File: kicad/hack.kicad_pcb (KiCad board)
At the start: 2 copper layers, 27 parts, among them P1 USB_micro, P2 CONN_01X13, P3 CONN_01X13, U1 NCP1117, U2 STF202, U3 ATSAMD21E, U4 MRF24J40MA, X1 MC-306

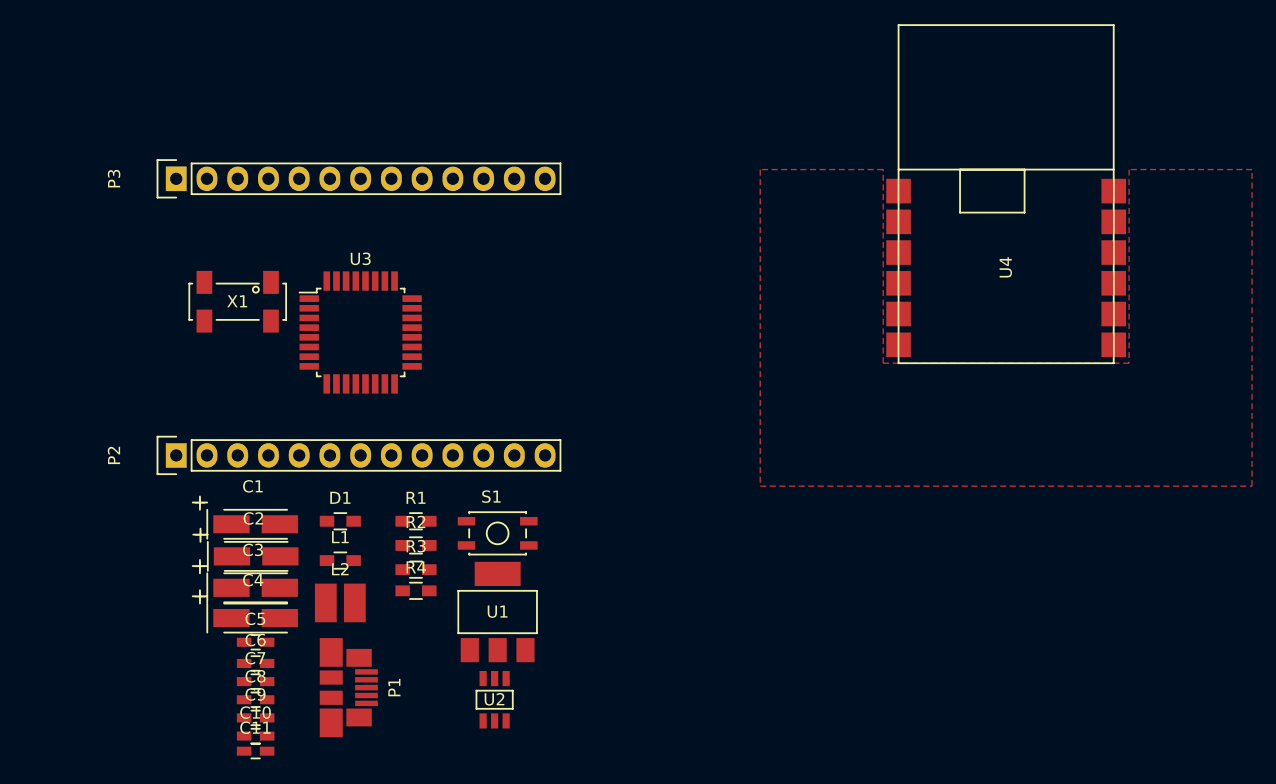
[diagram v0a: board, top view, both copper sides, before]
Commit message: Final components placement almost done
During this phase I checked if everything could fit in the board. It
didn't, so I found a replacement LDO (in a small 1.2x1.2mm DFN package)
that needs 2x0603 ceramic caps rather than two clunky electros (more
free space then) and I finally changed the D21E package to QFN as well,
now everything seems to fit quite well.
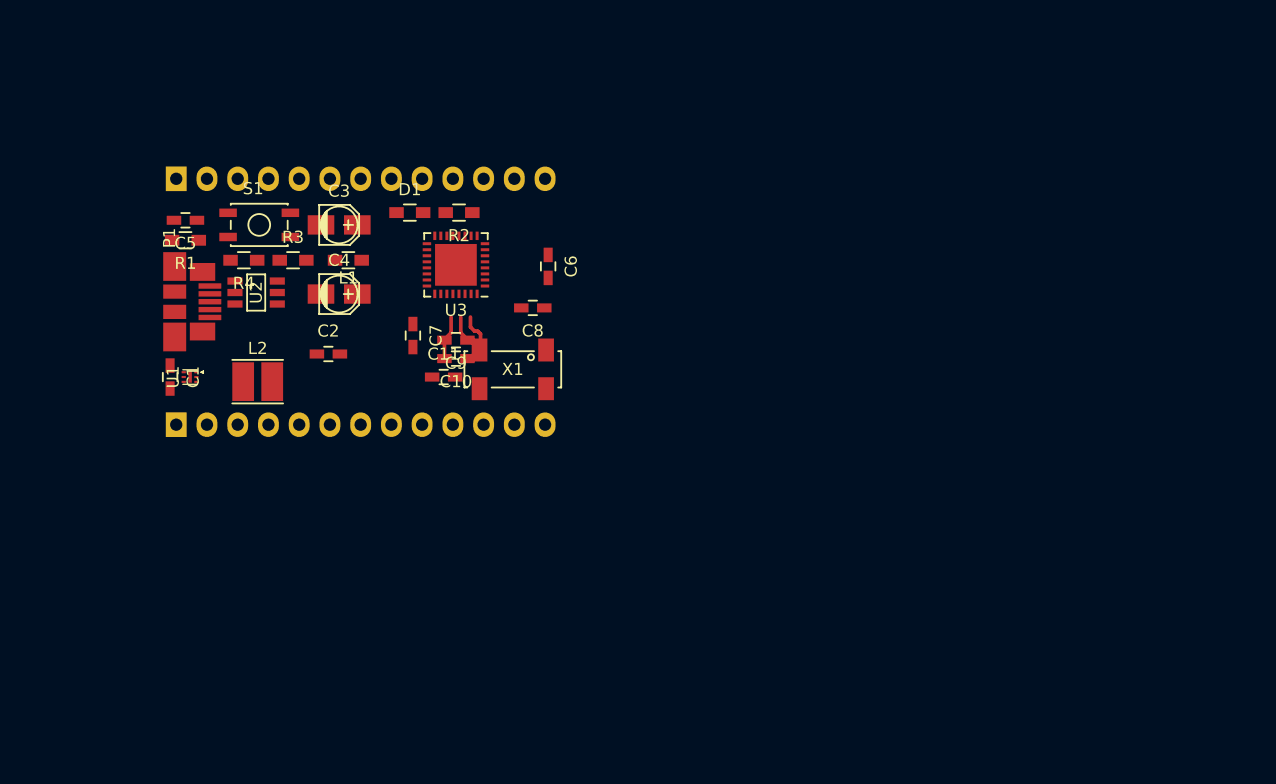
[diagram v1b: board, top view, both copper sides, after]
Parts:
- removed U4: MRF24J40MA, hack-footprints:MRF24J40MA
- C1, C2: value 10u -> 2.2u; footprint Capacitors_Tantalum_SMD:TantalC_SizeA_EIA-3216_HandSoldering -> Capacitors_SMD:C_0603_HandSoldering
- C3, C4: footprint Capacitors_Tantalum_SMD:TantalC_SizeA_EIA-3216_HandSoldering -> Capacitors_SMD:c_elec_3x5.3
- L2: footprint hack-footprints:ELLVFG -> ELLVFG
- P1: footprint hack-footprints:47346-0001 -> 47346-0001
- P2, P3: moved to B.Cu
- U1: value NCP1117 -> MIC5528; footprint hack-footprints:SOT-223 -> Housings_DFN_QFN:DFN-6-1EP_1.2x1.2mm_Pitch0.4mm
- U3: footprint Housings_QFP:TQFP-32_7x7mm_Pitch0.8mm -> QFN-32-1EP_5x5mm_Pitch0.5mm
- moved C6 40.8 mm to (185.7, 83.4), turned to 270 degrees
- moved C8 39.7 mm to (184.4, 86.9), turned to 180 degrees
- moved U2 39.0 mm to (161.5, 85.6), turned to 270 degrees
- moved C5 35.3 mm to (155.7, 79.6), turned to 180 degrees
- moved C9 35.3 mm to (178.1, 89.5), turned to 180 degrees
- moved C10 35.3 mm to (178.1, 91.1), turned to 180 degrees
- moved C11 34.6 mm to (177.0, 92.6)
- moved P1 34.4 mm to (154.8, 86.4)
- moved S1 32.2 mm to (161.8, 80.0)
- moved U1 32.0 mm to (156.1, 92.6), turned to 90 degrees
- moved C7 31.4 mm to (174.5, 89.2), turned to 270 degrees
- moved R4 30.8 mm to (160.5, 82.9), turned to 180 degrees
- moved C3 30.8 mm to (168.4, 80.0)
- moved R1 30.0 mm to (155.7, 81.3), turned to 180 degrees
- moved R2 27.7 mm to (178.3, 79.0), turned to 180 degrees
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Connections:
- net Net-(C3-Pad1) renamed VDDANA
- net Net-(C5-Pad2) renamed shield
- net Net-(C9-Pad1) renamed VDDCORE
- net USB-DM renamed USB-D-
- net USB-DP renamed USB-D+
- C1 pad 1: Net-(C1-Pad1) -> VBUS
- C2 pad 1: Net-(C2-Pad1) -> VDD
- L1 pad 1: Net-(L1-Pad1) -> VDD
- L2 pad 1: Net-(L2-Pad1) -> VDD
- P1 pad 1: Net-(P1-Pad1) -> VBUS
- R3 pad 2: Net-(R3-Pad2) -> VDDF
- U1 pad 1: GND -> VDD
- U1 pad 2: Net-(C2-Pad1) -> VDD
- U1 pad 3: Net-(C1-Pad1) -> GND
- U1 pad 4: Net-(C2-Pad1) -> Net-(U1-Pad4)
- U2 pad 1: Net-(P1-Pad1) -> VBUS
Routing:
- net GND: track 0.00 -> 6.60 mm
- net VDDCORE: track 0.00 -> 2.07 mm
- net VDDF: track 0.00 -> 1.44 mm
- removed copper zone on F.Cu, net GND
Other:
- net class Default: clearance 0.2 -> 0.1524; trace_width 0.25 -> 0.1524; via_dia 0.6 -> 0.508; via_drill 0.4 -> 0.3302
- net class Power added: clearance 0.1524, trace_width 0.3048, via_dia 0.5842, via_drill 0.3302
- rule trace_clearance: 0.2 -> 0.1524
- rule trace_min: 0.2 -> 0.1524
- rule via_min_drill: 0.3 -> 0.3302
- rule via_min_size: 0.4 -> 0.508

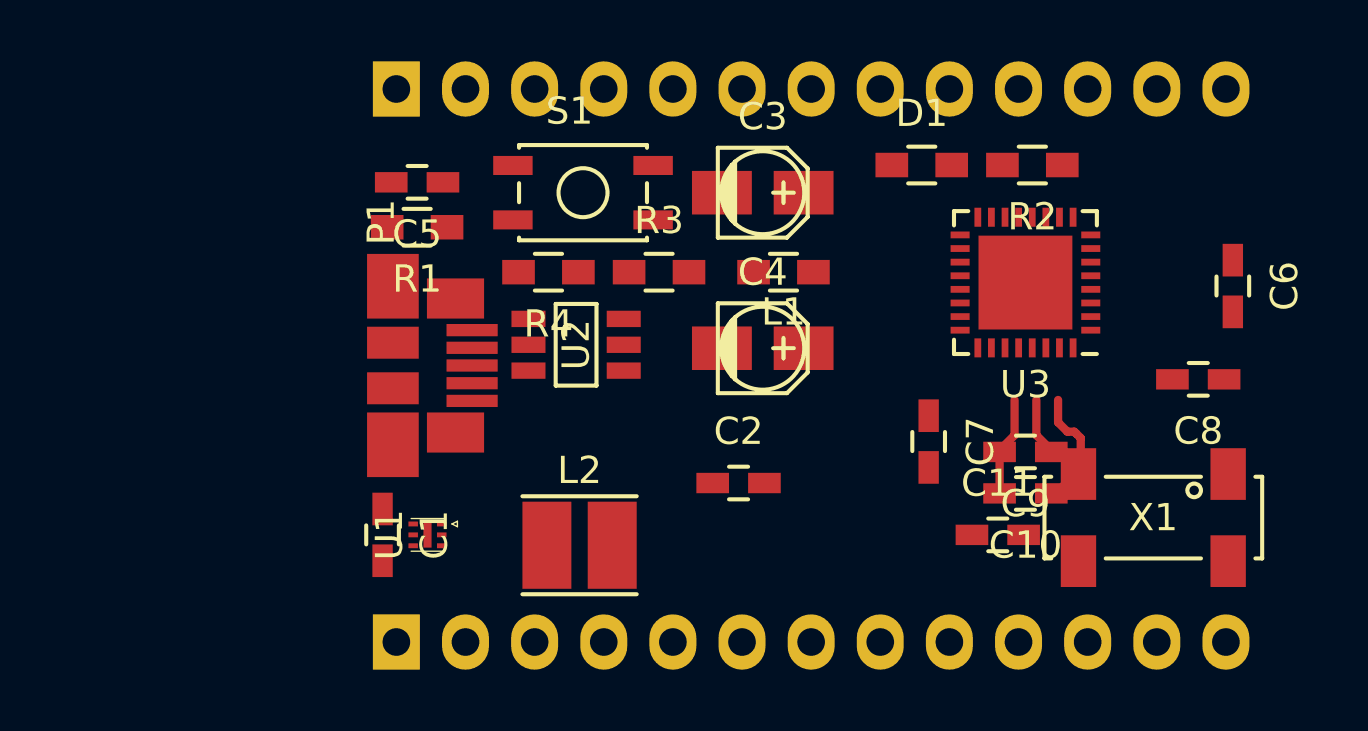
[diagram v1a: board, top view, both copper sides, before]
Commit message: Layout 99,9% finished
Nets 100% routed, need to double check if copper pours are all connected
to ground; added fiducials on board (for pick-n-place machines), I only
need to find a good spot for them
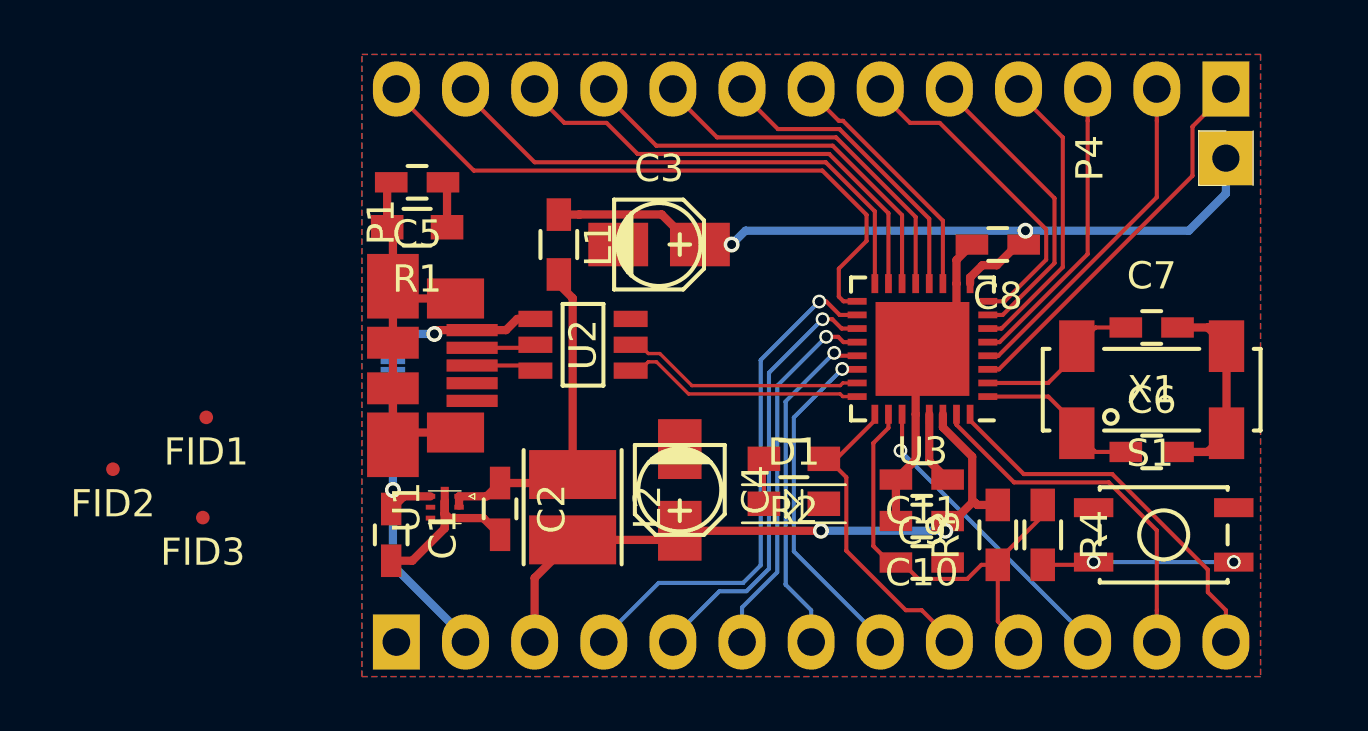
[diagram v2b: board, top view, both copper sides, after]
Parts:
- added FID1: FIDUCIAL, hack-footprints:FIDUCIAL, F.Cu at (148.0, 88.3)
- added FID2: FIDUCIAL, hack-footprints:FIDUCIAL, F.Cu at (144.5, 90.2)
- added FID3: FIDUCIAL, hack-footprints:FIDUCIAL, F.Cu at (147.8, 91.9)
- added JP1: Jumper_NO_Small, hack-footprints:SMD_Jumper, B.Cu at (154.8, 86.4)
- added P4: CONN_01X01, Pin_Headers:Pin_Header_Straight_1x01, F.Cu at (185.4, 78.7)
- D1: footprint Resistors_SMD:R_0603_HandSoldering -> hack-footprints:LED_0603_HandSoldering
- L1: footprint Resistors_SMD:R_0603_HandSoldering -> hack-footprints:L_0603_HandSoldering
- U1: footprint Housings_DFN_QFN:DFN-6-1EP_1.2x1.2mm_Pitch0.4mm -> hack-footprints:DFN-6-1EP_1.2x1.2mm_Pitch0.4mm
- moved P3 30.5 mm to (185.4, 76.2), turned to 90 degrees
- moved S1 24.8 mm to (183.1, 92.6)
- moved R4 20.6 mm to (178.7, 92.6), turned to 270 degrees
- moved R3 15.8 mm to (177.0, 92.6), turned to 90 degrees
- moved R2 13.9 mm to (169.5, 89.8)
- moved D1 13.3 mm to (169.5, 91.4)
- moved C7 9.20 mm to (182.7, 85.0), turned to 0 degrees
- moved C8 8.88 mm to (177.0, 81.9)
- moved C2 8.81 mm to (158.8, 91.6), turned to 270 degrees
- moved L1 8.32 mm to (160.9, 81.9), turned to 90 degrees
- moved C6 6.79 mm to (182.7, 89.5), turned to 0 degrees
- moved C4 6.03 mm to (165.4, 90.9), turned to 270 degrees
- moved X1 4.70 mm to (182.7, 87.2), turned to 0 degrees
- moved U3 4.50 mm to (174.3, 85.8)
- moved C3 4.26 mm to (164.6, 81.9)
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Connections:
- C1 pad 1: VBUS -> VLDO
- D1 pad 1: GND -> Net-(D1-Pad1)
- D1 pad 2: Net-(D1-Pad2) -> GND
- P2 pad 1: Net-(P2-Pad1) -> GND
- P2 pad 10: Net-(P2-Pad10) -> !RESET
- P2 pad 11: Net-(P2-Pad11) -> PA28
- P2 pad 12: Net-(P2-Pad12) -> PA30/SWCLK
- P2 pad 13: Net-(P2-Pad13) -> PA31/SWDIO
- P2 pad 2: Net-(P2-Pad2) -> VLDO
- P2 pad 3: Net-(P2-Pad3) -> VDDF
- P2 pad 4: Net-(P2-Pad4) -> PA17
- P2 pad 5: Net-(P2-Pad5) -> PA18
- P2 pad 6: Net-(P2-Pad6) -> PA19
- P2 pad 7: Net-(P2-Pad7) -> PA22
- P2 pad 8: Net-(P2-Pad8) -> PA23
- P2 pad 9: Net-(P2-Pad9) -> PA27
- P3 pad 1: Net-(P3-Pad1) -> PA02/A
- P3 pad 10: Net-(P3-Pad10) -> PA11
- P3 pad 11: Net-(P3-Pad11) -> PA14
- P3 pad 12: Net-(P3-Pad12) -> PA15
- P3 pad 13: Net-(P3-Pad13) -> PA16
- P3 pad 2: Net-(P3-Pad2) -> PA03/A
- P3 pad 3: Net-(P3-Pad3) -> PA04/A
- P3 pad 4: Net-(P3-Pad4) -> PA05/A
- P3 pad 5: Net-(P3-Pad5) -> PA06/A
- P3 pad 6: Net-(P3-Pad6) -> PA07/A
- P3 pad 7: Net-(P3-Pad7) -> PA08
- P3 pad 8: Net-(P3-Pad8) -> PA09
- P3 pad 9: Net-(P3-Pad9) -> PA10
- R2 pad 1: PA28 -> PA27
- R2 pad 2: Net-(D1-Pad2) -> Net-(D1-Pad1)
- U1 pad 6: VBUS -> VLDO
- U3 pad 33: (no net) -> GND
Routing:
- net VDDANA: track 0.00 -> 30.3 mm, vias 0 -> 2
- net PA16: track 0.00 -> 23.5 mm
- net VDDF: track 1.44 -> 24.4 mm, vias 0 -> 2
- net PA15: track 0.00 -> 19.6 mm
- net PA17: track 0.00 -> 19.2 mm, vias 0 -> 1
- net GND: track 6.60 -> 25.2 mm
- net PA14: track 0.00 -> 17.6 mm
- net !RESET: track 0.00 -> 16.4 mm
- net PA18: track 0.00 -> 16.1 mm, vias 0 -> 1
- net PA11: track 0.00 -> 15.5 mm
- net shield: track 0.00 -> 14.8 mm
- net PA31/SWDIO: track 0.00 -> 14.2 mm
- net PA02/A: track 0.00 -> 14.2 mm
- net PA19: track 0.00 -> 13.7 mm, vias 0 -> 1
- net PA30/SWCLK: track 0.00 -> 13.5 mm
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- added copper zone on B.Cu, net GND
- added copper zone on F.Cu, net GND

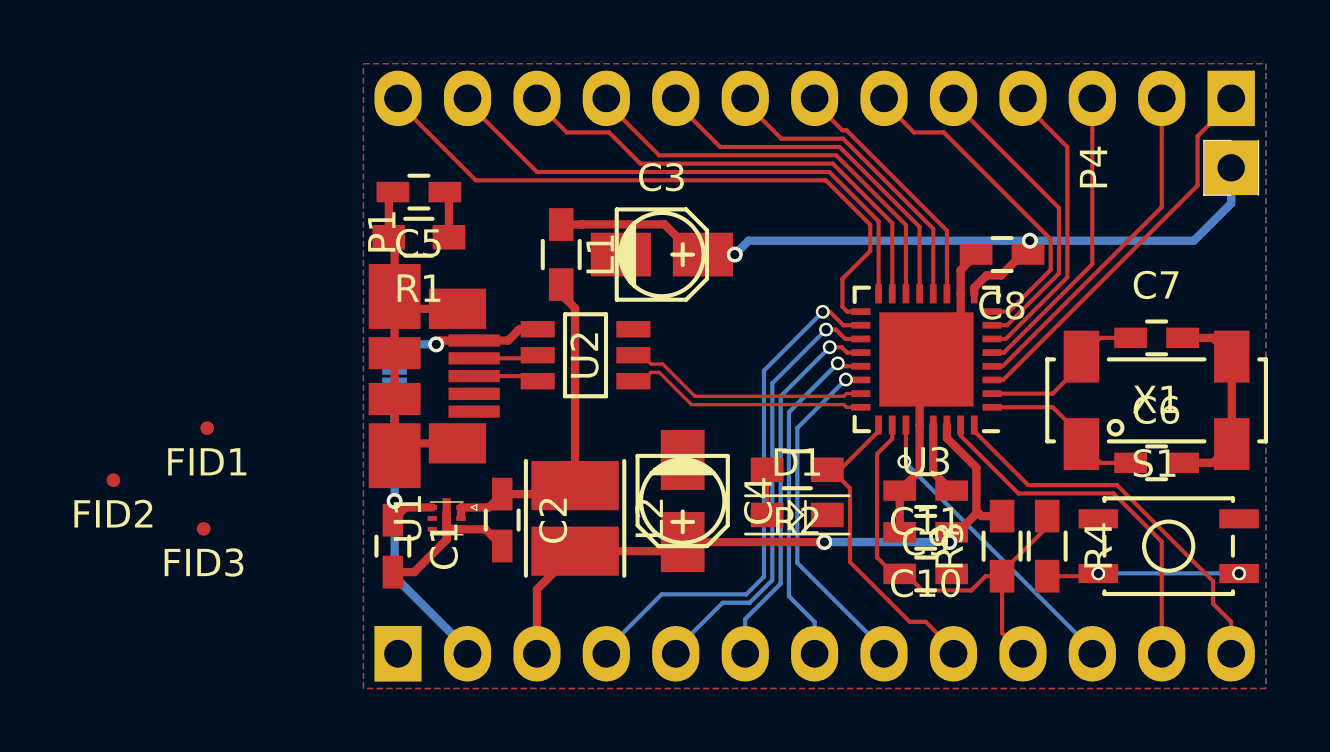
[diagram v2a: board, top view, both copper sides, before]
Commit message: Cleaning up before test run
Removed obsolete Eagle CAD files, added OSHW/Hackaday logos on schematic
and silkscreen, removed ground connections for pins 2-3 of 32.768 KHz
XTAL, removed traces under USB data lines, moving analog lines around
(not beneath) XTAL (w.i.p.), moved components names on silkscreen to be
readable, set fiducials in position, fixed SPST SMD package
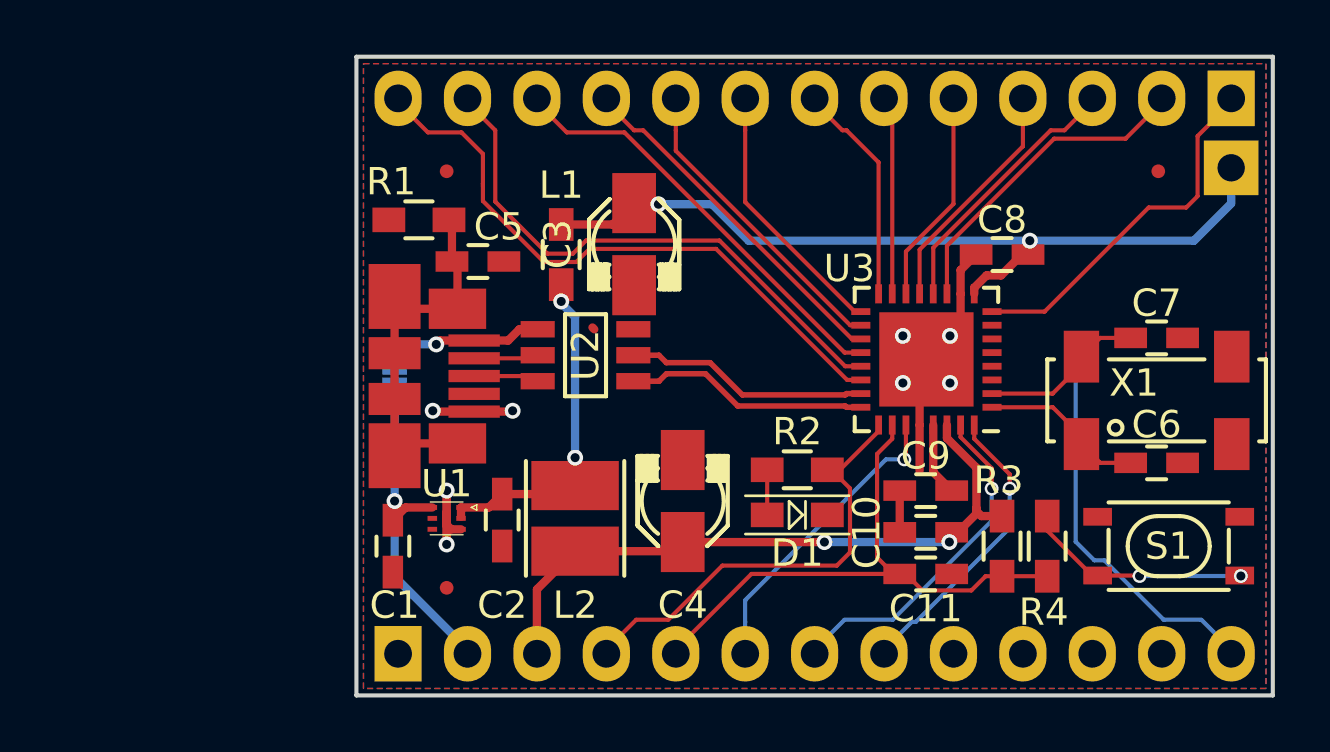
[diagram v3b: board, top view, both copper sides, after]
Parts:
- added LOGO1: OSHW, hack-footprints:OSHW-LOGO, B.Cu at (164.3, 90.4)
- added LOGO2: HACKADAY, hack-footprints:HACKADAY-LOGO, B.Cu at (182.1, 90.4)
- C3, C4: footprint Capacitors_SMD:c_elec_3x5.3 -> hack-footprints:c_elec_3x5.3
- FID3: footprint hack-footprints:FIDUCIAL -> FIDUCIAL
- P4: moved to B.Cu
- S1: footprint Buttons_Switches_SMD:SW_SPST_EVQP2 -> hack-footprints:SPST
- moved FID3 37.3 mm to (182.8, 78.9)
- moved FID2 16.6 mm to (156.7, 78.9)
- moved FID1 10.5 mm to (156.7, 94.1)
- moved C5 3.33 mm to (157.9, 82.2)
- moved C3 1.09 mm to (163.6, 81.5), turned to 180 degrees
- moved R1 0.64 mm to (155.7, 80.6), turned to 0 degrees
- turned C4 to 0 degrees
- turned P4 to 270 degrees
- turned R4 to 90 degrees
- turned S1 to 270 degrees
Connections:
- X1 pad 2: GND -> Net-(X1-Pad2)
- X1 pad 3: GND -> Net-(X1-Pad3)
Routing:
- net PA30/SWCLK: track 13.5 -> 0.59 mm
- net PA11: track 15.5 -> 3.47 mm
- net PA19: track 13.7 -> 1.76 mm, vias 1 -> 0
- net PA23: track 12.6 -> 24.2 mm
- net GND: track 25.2 -> 14.4 mm, vias 0 -> 8
- net PA16: track 23.5 -> 14.9 mm
- net PA27: track 11.8 -> 4.10 mm
- net PA17: track 19.2 -> 13.4 mm, vias 1 -> 0
- net PA09: track 11.3 -> 5.63 mm
- net PA15: track 19.6 -> 24.7 mm
- net PA06/A: track 11.2 -> 6.48 mm
- net PA08: track 9.25 -> 5.15 mm
- net PA05/A: track 10.9 -> 7.25 mm
- net PA04/A: track 11.1 -> 8.17 mm
- net PA07/A: track 12.2 -> 9.35 mm
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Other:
- board outline added: 33.5 x 23.4 mm
- net class USB added: clearance 0.1524, trace_width 0.254, via_dia 0.508, via_drill 0.3302
- board text added: "VLDO=VBUS"
